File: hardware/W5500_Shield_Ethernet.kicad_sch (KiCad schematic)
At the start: 33 parts, among them J1 HR911105A, J2 Conn_02x05_Odd_Even, U2 W5500, Y1 X322525MOB4SI

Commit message: schematics and photos
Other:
- moved on the sheet: C10, C11, C12, C13, C14, C15, C3, C4, C5, C6, C7, C8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

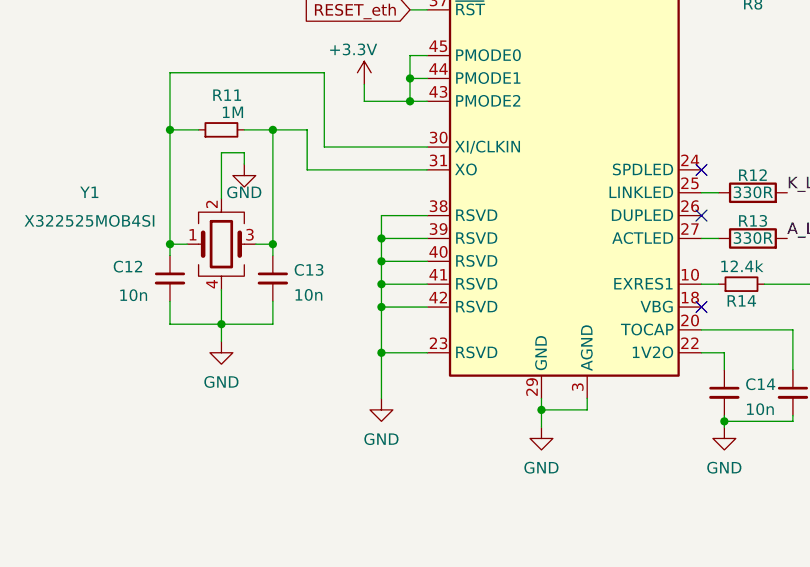
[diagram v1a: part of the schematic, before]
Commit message: RSVD pins
Estaban conectados a gnd y se dejaron al aire como indica el datasheet
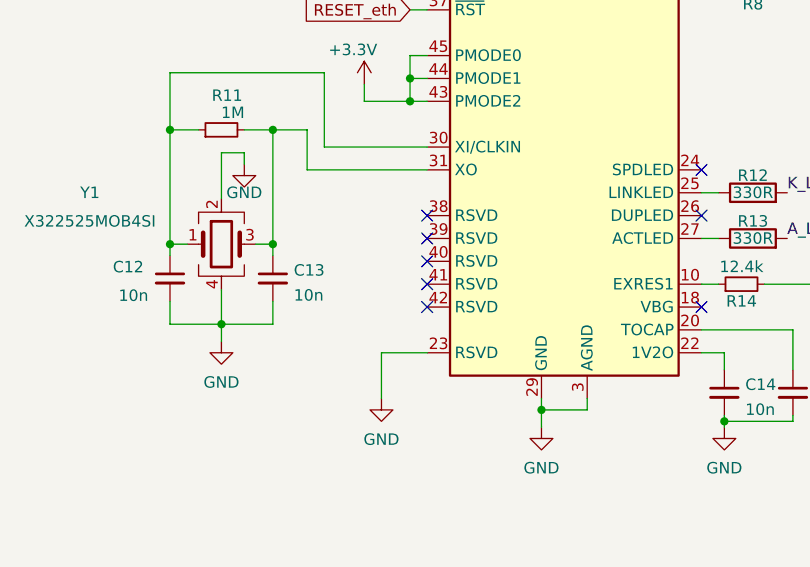
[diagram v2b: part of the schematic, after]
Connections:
- net GND: no longer U2.38 (RSVD), U2.39 (RSVD), U2.40 (RSVD), U2.41 (RSVD), U2.42 (RSVD)
- no-connect marks 3 -> 8
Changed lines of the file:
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@@
   (junction (at 93.98 134.62) (diameter 0) (color 0 0 0 0)
   )
-  (junction (at 76.2 115.57) (diameter 0) (color 0 0 0 0)
-  )
   (junction (at 58.42 125.095) (diameter 0) (color 0 0 0 0)
   )
-  (junction (at 76.2 123.19) (diameter 0) (color 0 0 0 0)
-  )
   (junction (at 114.3 135.89) (diameter 0) (color 0 0 0 0)
   )
   (junction (at 115.57 67.31) (diameter 0) (color 0 0 0 0)
   )
-  (junction (at 76.2 120.65) (diameter 0) (color 0 0 0 0)
-  )
   (junction (at 137.795 99.06) (diameter 0) (color 0 0 0 0)
   )
-  (junction (at 76.2 118.11) (diameter 0) (color 0 0 0 0)
-  )
   (junction (at 137.795 87.63) (diameter 0) (color 0 0 0 0)
   )
@@
   )
   (junction (at 209.55 35.56) (diameter 0) (color 0 0 0 0)
-  )
-  (junction (at 76.2 128.27) (diameter 0) (color 0 0 0 0)
   )
   (junction (at 131.445 85.09) (diameter 0) (color 0 0 0 0)
@@
   (no_connect (at 111.76 113.03))
   (no_connect (at 111.76 123.19))
+  (no_connect (at 81.28 113.03))
+  (no_connect (at 81.28 123.19))
+  (no_connect (at 81.28 120.65))
+  (no_connect (at 81.28 118.11))
+  (no_connect (at 81.28 115.57))
   (wire (pts (xy 237.49 102.87) (xy 237.49 104.14))
     (stroke (width 0) (type default) (color 0 0 0 0))
@@
     (stroke (width 0) (type default) (color 0 0 0 0))
   )
-  (wire (pts (xy 76.2 115.57) (xy 76.2 118.11))
-    (stroke (width 0) (type default) (color 0 0 0 0))
-  )
   (wire (pts (xy 131.445 85.09) (xy 146.685 85.09))
     (stroke (width 0) (type default) (color 0 0 0 0))
@@
     (stroke (width 0) (type default) (color 0 0 0 0))
   )
-  (wire (pts (xy 81.28 118.11) (xy 76.2 118.11))
-    (stroke (width 0) (type default) (color 0 0 0 0))
-  )
   (wire (pts (xy 76.835 59.055) (xy 93.98 59.055))
     (stroke (width 0) (type default) (color 0 0 0 0))
@@
     (stroke (width 0) (type default) (color 0 0 0 0))
   )
-  (wire (pts (xy 76.2 120.65) (xy 76.2 123.19))
-    (stroke (width 0) (type default) (color 0 0 0 0))
-  )
   (wire (pts (xy 153.67 128.905) (xy 149.86 128.905))
     (stroke (width 0) (type default) (color 0 0 0 0))
@@
     (stroke (width 0) (type default) (color 0 0 0 0))
   )
-  (wire (pts (xy 76.2 118.11) (xy 76.2 120.65))
-    (stroke (width 0) (type default) (color 0 0 0 0))
-  )
   (wire (pts (xy 209.55 35.56) (xy 209.55 38.1))
     (stroke (width 0) (type default) (color 0 0 0 0))
@@
     (stroke (width 0) (type default) (color 0 0 0 0))
   )
-  (wire (pts (xy 76.2 120.65) (xy 81.28 120.65))
-    (stroke (width 0) (type default) (color 0 0 0 0))
-  )
   (wire (pts (xy 58.42 125.095) (xy 52.705 125.095))
     (stroke (width 0) (type default) (color 0 0 0 0))
@@
     (stroke (width 0) (type default) (color 0 0 0 0))
   )
-  (wire (pts (xy 81.28 113.03) (xy 76.2 113.03))
-    (stroke (width 0) (type default) (color 0 0 0 0))
-  )
   (wire (pts (xy 115.57 67.31) (xy 115.57 69.85))
     (stroke (width 0) (type default) (color 0 0 0 0))
@@
     (stroke (width 0) (type default) (color 0 0 0 0))
   )
-  (wire (pts (xy 76.2 123.19) (xy 81.28 123.19))
-    (stroke (width 0) (type default) (color 0 0 0 0))
-  )
   (wire (pts (xy 134.62 77.47) (xy 154.305 77.47))
     (stroke (width 0) (type default) (color 0 0 0 0))
@@
     (stroke (width 0) (type default) (color 0 0 0 0))
   )
-  (wire (pts (xy 76.2 115.57) (xy 81.28 115.57))
-    (stroke (width 0) (type default) (color 0 0 0 0))
-  )
   (wire (pts (xy 140.97 66.04) (xy 140.97 67.31))
     (stroke (width 0) (type default) (color 0 0 0 0))
@@
     (stroke (width 0) (type default) (color 0 0 0 0))
   )
-  (wire (pts (xy 76.2 123.19) (xy 76.2 128.27))
-    (stroke (width 0) (type default) (color 0 0 0 0))
-  )
   (wire (pts (xy 162.56 78.74) (xy 175.26 78.74))
     (stroke (width 0) (type default) (color 0 0 0 0))
@@
     (stroke (width 0) (type default) (color 0 0 0 0))
   )
-  (wire (pts (xy 76.2 113.03) (xy 76.2 115.57))
-    (stroke (width 0) (type default) (color 0 0 0 0))
-  )
